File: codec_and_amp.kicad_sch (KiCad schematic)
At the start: 39 parts, among them J1 Conn_01x10, J2 Conn_01x06, U1 TLV320AIC3206IRSBR, U4 FSA2275UMX, U6 MIC5504-1.8YM5, U7 TPD4E02B04DQAR, U8 TPD4E02B04DQAR

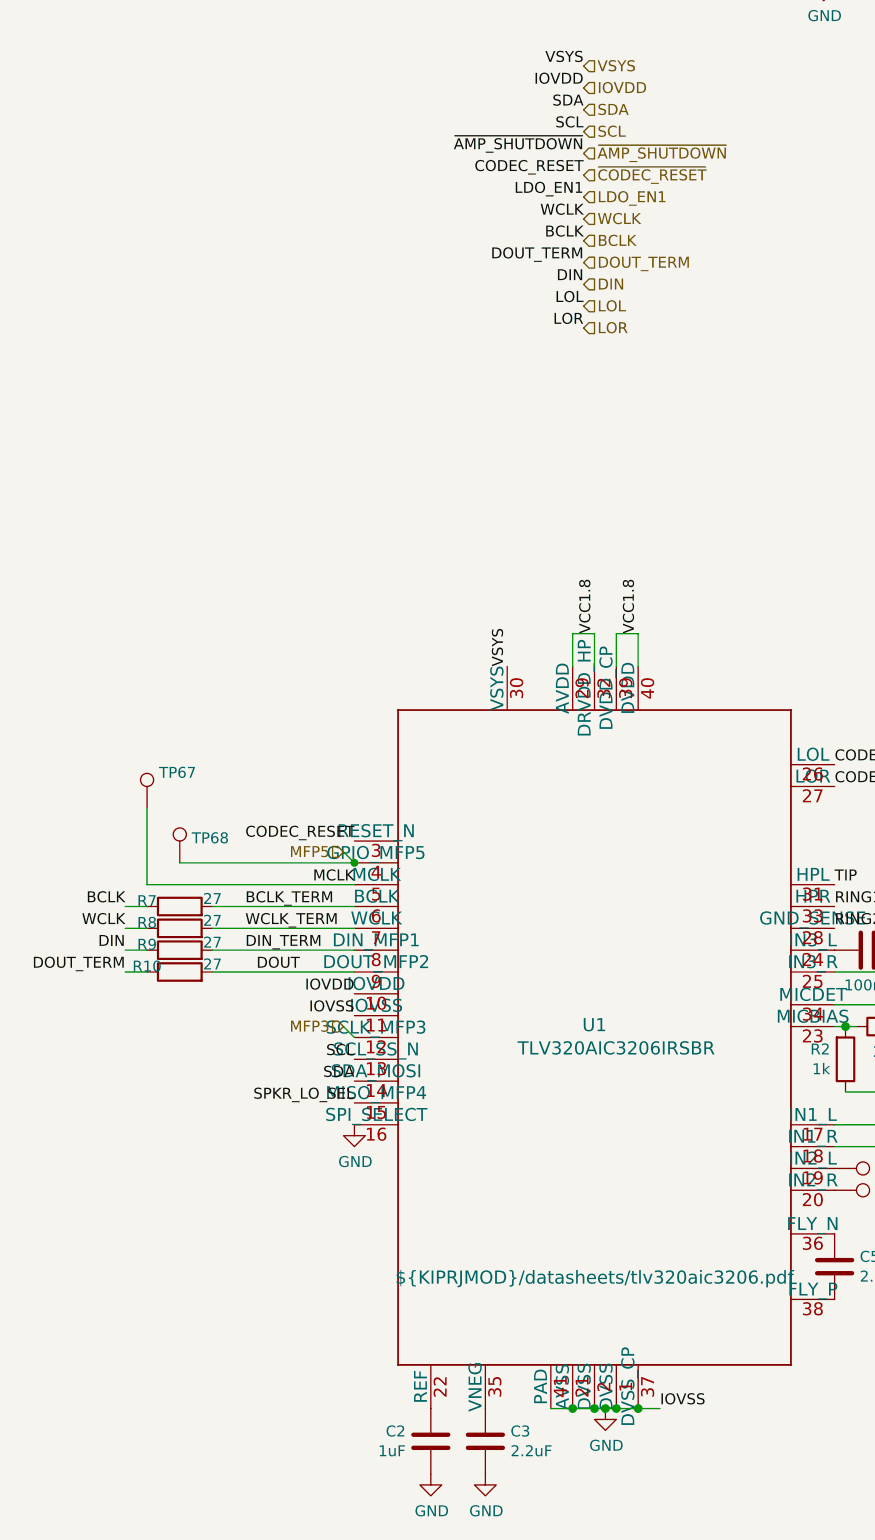
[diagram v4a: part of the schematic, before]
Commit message: Fix most ERC errors; cleanup silkscreen and comment layers.
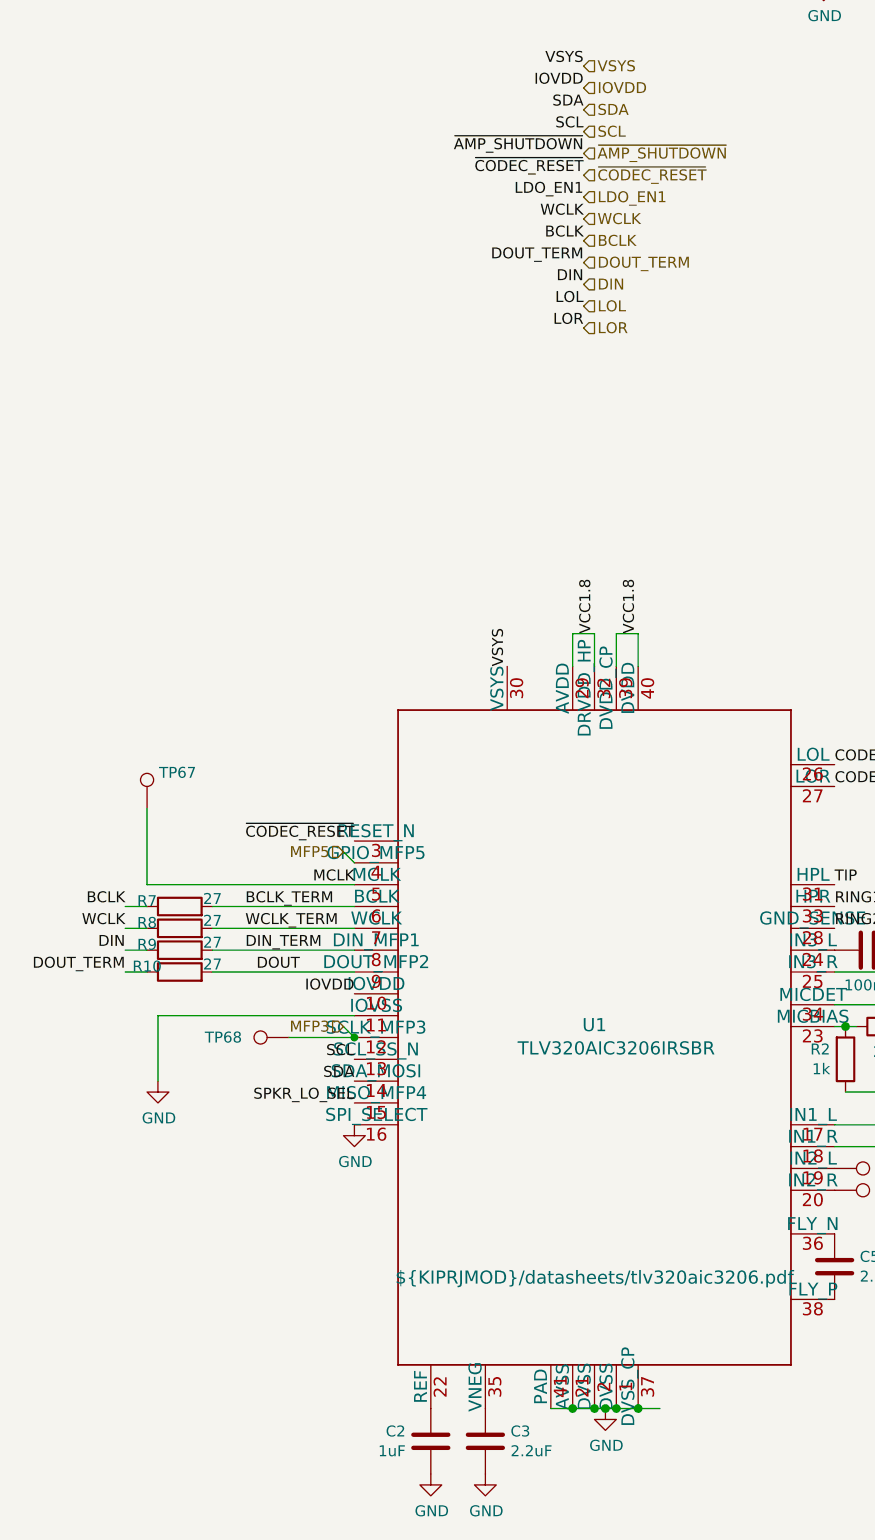
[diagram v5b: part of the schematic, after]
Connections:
- net MFP3: now also TP68.1
- net MFP5: no longer TP68.1
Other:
- moved on the sheet: TP68
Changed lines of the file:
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@@
   (junction (at 274.32 92.71) (diameter 1.016) (color 0 0 0 0)
   )
-  (junction (at 57.15 158.75) (diameter 0) (color 0 0 0 0)
-  )
   (junction (at 299.72 90.17) (diameter 1.016) (color 0 0 0 0)
   )
@@
   )
   (junction (at 317.5 102.87) (diameter 1.016) (color 0 0 0 0)
+  )
+  (junction (at 57.15 179.07) (diameter 0) (color 0 0 0 0)
   )
   (junction (at 287.02 147.32) (diameter 1.016) (color 0 0 0 0)
@@
     (stroke (width 0) (type solid) (color 0 0 0 0))
   )
+  (wire (pts (xy 34.29 176.53) (xy 57.15 176.53))
+    (stroke (width 0) (type default) (color 0 0 0 0))
+  )
   (wire (pts (xy 304.8 130.81) (xy 304.8 95.25))
     (stroke (width 0) (type solid) (color 0 0 0 0))
@@
   (wire (pts (xy 276.86 130.81) (xy 271.78 130.81))
     (stroke (width 0) (type solid) (color 0 0 0 0))
+  )
+  (wire (pts (xy 49.53 179.07) (xy 57.15 179.07))
+    (stroke (width 0) (type default) (color 0 0 0 0))
   )
   (wire (pts (xy 274.32 128.27) (xy 274.32 92.71))
@@
     (stroke (width 0) (type solid) (color 0 0 0 0))
   )
+  (wire (pts (xy 34.29 176.53) (xy 34.29 184.15))
+    (stroke (width 0) (type default) (color 0 0 0 0))
+  )
   (wire (pts (xy 238.76 116.84) (xy 223.52 116.84))
     (stroke (width 0) (type solid) (color 0 0 0 0))
@@
   (wire (pts (xy 264.16 60.96) (xy 259.08 60.96))
     (stroke (width 0) (type solid) (color 0 0 0 0))
-  )
-  (wire (pts (xy 36.83 158.75) (xy 57.15 158.75))
-    (stroke (width 0) (type default) (color 0 0 0 0))
   )
   (wire (pts (xy 265.43 100.33) (xy 320.04 100.33))
@@
     (effects (font (size 1.27 1.27)) (justify left bottom))
   )
-  (label "IOVSS" (at 92.71 222.25 0)
-    (effects (font (size 1.27 1.27)) (justify left bottom))
-  )
   (label "VCC1.8" (at 312.42 39.37 0)
     (effects (font (size 1.27 1.27)) (justify left bottom))
@@
     (effects (font (size 1.27 1.27)) (justify right bottom))
   )
-  (label "IOVSS" (at 57.15 176.53 180)
-    (effects (font (size 1.27 1.27)) (justify right bottom))
-  )
   (label "VSYS" (at 74.93 135.89 90)
     (effects (font (size 1.27 1.27)) (justify left bottom))
@@
     (effects (font (size 1.27 1.27)) (justify right bottom))
   )
-  (label "CODEC_RESET" (at 83.82 78.74 180)
+  (label "~{CODEC_RESET}" (at 83.82 78.74 180)
     (effects (font (size 1.27 1.27)) (justify right bottom))
   )
@@
     (effects (font (size 1.27 1.27)) (justify left bottom))
   )
-  (label "CODEC_RESET" (at 57.15 156.21 180)
+  (label "~{CODEC_RESET}" (at 57.15 156.21 180)
     (effects (font (size 1.27 1.27)) (justify right bottom))
   )
@@
     (pin "5")
   )
-  (symbol (lib_id "Connector:TestPoint") (at 36.83 158.75 0) (unit 1)
-    (in_bom yes) (on_board yes) (fields_autoplaced)
-    (property "Reference" "TP68" (id 0) (at 38.227 155.8818 0)
-      (effects (font (size 1.27 1.27)) (justify left))
-    )
-    (property "Value" "TestPoint" (id 1) (at 38.227 157.1502 0)
+  (symbol (lib_id "Connector:TestPoint") (at 49.53 179.07 90) (unit 1)
+    (in_bom yes) (on_board yes)
+    (property "Reference" "TP68" (id 0) (at 41.91 179.07 90))
+    (property "Value" "TestPoint" (id 1) (at 47.9302 177.673 0)
       (effects (font (size 1.27 1.27)) (justify left) hide)
     )
-    (property "Footprint" "footprints:testpoint_small" (id 2) (at 41.91 158.75 0)
-      (effects (font (size 1.27 1.27)) hide)
-    )
-    (property "Datasheet" "~" (id 3) (at 41.91 158.75 0)
+    (property "Footprint" "footprints:testpoint_small" (id 2) (at 49.53 173.99 0)
+      (effects (font (size 1.27 1.27)) hide)
+    )
+    (property "Datasheet" "~" (id 3) (at 49.53 173.99 0)
       (effects (font (size 1.27 1.27)) hide)
     )
@@
       (effects (font (size 1.27 1.27)) hide)
     )
+    (pin "1")
+  )
+  (symbol (lib_id "power:GND") (at 34.29 184.15 0) (unit 1)
+    (in_bom yes) (on_board yes)
+    (property "Reference" "#PWR0153" (id 0) (at 34.29 190.5 0)
+      (effects (font (size 1.27 1.27)) hide)
+    )
+    (property "Value" "GND" (id 1) (at 34.4043 188.4744 0))
+    (property "Footprint" "" (id 2) (at 34.29 184.15 0)
+      (effects (font (size 1.27 1.27)) hide)
+    )
+    (property "Datasheet" "" (id 3) (at 34.29 184.15 0)
+      (effects (font (size 1.27 1.27)) hide)
+    )

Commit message: Board rev2 ready to order, hopefully
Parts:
- added TP151: TestPoint, footprints:testpoint_small, symbol Connector:TestPoint
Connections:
- net GND: now also TP151.1
- net MICBIAS: now reaches R1.1, R2.2, U1.23 (MICBIAS)
- net IN3_L: now reaches C1.1, U1.24 (IN3_L)
- net FLY_N: now reaches C5.1, U1.36 (FLY_N)
- net FLY_P: now reaches C5.2, U1.38 (FLY_P)
- net IN2_L: now reaches TP69.1, U1.19 (IN2_L)
- net INTMIC_P_bypass: now reaches C12.1, R2.1, U1.18 (IN1_R)
- net V_C_EXT: now reaches C22.1, U4.2 (C_EXT)
- net INTMIC_N_bypass: now reaches C9.1, R3.1, U1.17 (IN1_L)
- net IN2_R: now reaches TP70.1, U1.20 (IN2_R)
- net MUTE: now reaches R6.1, U4.7 (MUTE)
- net VNEG: now reaches C3.1, U1.35 (VNEG)
- net VREF: now reaches C2.1, U1.22 (REF)
- net IN3_R: now reaches TP71.1, U1.25 (IN3_R)
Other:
- moved on the sheet: C1, C12, C2, C3, C9, R1, R2, R3, TP69, TP70
